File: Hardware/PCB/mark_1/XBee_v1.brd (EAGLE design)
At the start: 30.5 x 34.3 mm, 17 parts, among them IC1 4050, IC2 LM1117S

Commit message: 
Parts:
- renumbered U$1 to IC3
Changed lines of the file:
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@@
 <attribute name="VALUE" x="22.86" y="14.605" size="1.27" layer="28" rot="MR270"/>
 </element>
-<element name="U$1" library="mark_1" package="XBEE-1" value="XBEE-1B1" x="15.24" y="5.08" smashed="yes"/>
+<element name="IC3" library="mark_1" package="XBEE-1" value="XBEE-1B1" x="15.24" y="5.08" smashed="yes"/>
 <element name="JP1" library="mark_1" package="1X02" value="" x="7.62" y="11.43" smashed="yes" rot="R270">
 <attribute name="VALUE" x="4.445" y="13.97" size="1.27" layer="27" rot="R270"/>
@@
 <attribute name="VALUE" x="24.13" y="29.464" size="1.27" layer="28" ratio="10" rot="MR0"/>
 </element>
-<element name="JP2" library="mark_1" package="1X01" value="TXD" x="7.62" y="25.4" smashed="yes" rot="R270">
-<attribute name="VALUE" x="8.89" y="24.765" size="1.27" layer="27"/>
-</element>
-<element name="JP3" library="mark_1" package="1X01" value="RXD" x="7.62" y="22.86" smashed="yes" rot="R270">
-<attribute name="VALUE" x="8.89" y="22.225" size="1.27" layer="27"/>
-</element>
-<element name="JP4" library="mark_1" package="1X01" value="RST" x="7.62" y="20.32" smashed="yes" rot="R270">
-<attribute name="VALUE" x="8.89" y="19.685" size="1.27" layer="27"/>
-</element>
-<element name="JP5" library="mark_1" package="1X01" value="RSSI" x="7.62" y="15.24" smashed="yes">
-<attribute name="VALUE" x="8.89" y="14.605" size="1.27" layer="27"/>
-</element>
-<element name="JP6" library="mark_1" package="1X01" value="DTR" x="7.62" y="17.78" smashed="yes" rot="R270">
-<attribute name="VALUE" x="8.89" y="17.145" size="1.27" layer="27"/>
-</element>
-<element name="JP7" library="mark_1" package="1X01" value="CTS" x="7.62" y="5.08" smashed="yes" rot="R90">
-<attribute name="VALUE" x="8.89" y="4.445" size="1.27" layer="27"/>
-</element>
-<element name="JP8" library="mark_1" package="1X01" value="RTS" x="7.62" y="7.62" smashed="yes" rot="R270">
-<attribute name="VALUE" x="8.89" y="6.985" size="1.27" layer="27"/>
-</element>
+<element name="JP2" library="mark_1" package="1X01" value="TXD" x="7.62" y="25.4" smashed="yes" rot="R270"/>
+<element name="JP3" library="mark_1" package="1X01" value="RXD" x="7.62" y="22.86" smashed="yes" rot="R270"/>
+<element name="JP4" library="mark_1" package="1X01" value="RST" x="7.62" y="20.32" smashed="yes" rot="R270"/>
+<element name="JP5" library="mark_1" package="1X01" value="RSSI" x="7.62" y="15.24" smashed="yes"/>
+<element name="JP6" library="mark_1" package="1X01" value="DTR" x="7.62" y="17.78" smashed="yes" rot="R270"/>
+<element name="JP7" library="mark_1" package="1X01" value="CTS" x="7.62" y="5.08" smashed="yes" rot="R90"/>
+<element name="JP8" library="mark_1" package="1X01" value="RTS" x="7.62" y="7.62" smashed="yes" rot="R270"/>
 </elements>
 <signals>
@@
 <contactref element="JP1" pad="2"/>
 <contactref element="LED1" pad="K"/>
-<contactref element="U$1" pad="10"/>
+<contactref element="IC3" pad="10"/>
 <contactref element="LED2" pad="K"/>
 <contactref element="IC1" pad="8"/>
@@
 <contactref element="IC2" pad="2"/>
 <contactref element="IC2" pad="4"/>
-<contactref element="U$1" pad="1"/>
+<contactref element="IC3" pad="1"/>
 <contactref element="IC1" pad="1"/>
 <contactref element="C1" pad="2"/>
@@
 </signal>
 <signal name="N$3">
-<contactref element="U$1" pad="3"/>
+<contactref element="IC3" pad="3"/>
 <contactref element="IC1" pad="6"/>
 <wire x1="14.7066" y1="22.86" x2="10.795" y2="22.86" width="0.4064" layer="16"/>
@@
 </signal>
 <signal name="N$4">
-<contactref element="U$1" pad="5"/>
+<contactref element="IC3" pad="5"/>
 <contactref element="IC1" pad="4"/>
 <wire x1="4.24" y1="17.08" x2="4.38" y2="17.08" width="0.4064" layer="16"/>
@@
 </signal>
 <signal name="RSSI">
-<contactref element="U$1" pad="6"/>
+<contactref element="IC3" pad="6"/>
 <contactref element="R1" pad="2"/>
 <contactref element="JP5" pad="1"/>
@@
 </signal>
 <signal name="N$7">
-<contactref element="U$1" pad="9"/>
+<contactref element="IC3" pad="9"/>
 <contactref element="IC1" pad="2"/>
 <wire x1="12.7" y1="17.78" x2="14.7066" y2="17.78" width="0.4064" layer="16"/>
@@
 </signal>
 <signal name="N$8">
-<contactref element="U$1" pad="16"/>
+<contactref element="IC3" pad="16"/>
 <contactref element="IC1" pad="10"/>
 <wire x1="26.24" y1="17.08" x2="25.465" y2="17.08" width="0.4064" layer="16"/>
@@
 </signal>
 <signal name="N$10">
-<contactref element="U$1" pad="15"/>
+<contactref element="IC3" pad="15"/>
 <contactref element="R2" pad="2"/>
 <wire x1="26.24" y1="15.08" x2="27.145" y2="15.08" width="0.4064" layer="16"/>
@@
 </signal>
 <signal name="TXD">
-<contactref element="U$1" pad="2"/>
+<contactref element="IC3" pad="2"/>
 <contactref element="JP2" pad="1"/>
 <wire x1="4.24" y1="23.08" x2="5.3" y2="23.08" width="0.4064" layer="16"/>
@@
 </signal>
 <signal name="CTS">
-<contactref element="U$1" pad="12"/>
+<contactref element="IC3" pad="12"/>
 <contactref element="JP7" pad="1"/>
 <wire x1="7.62" y1="5.08" x2="7.62" y2="2.54" width="0.4064" layer="16"/>

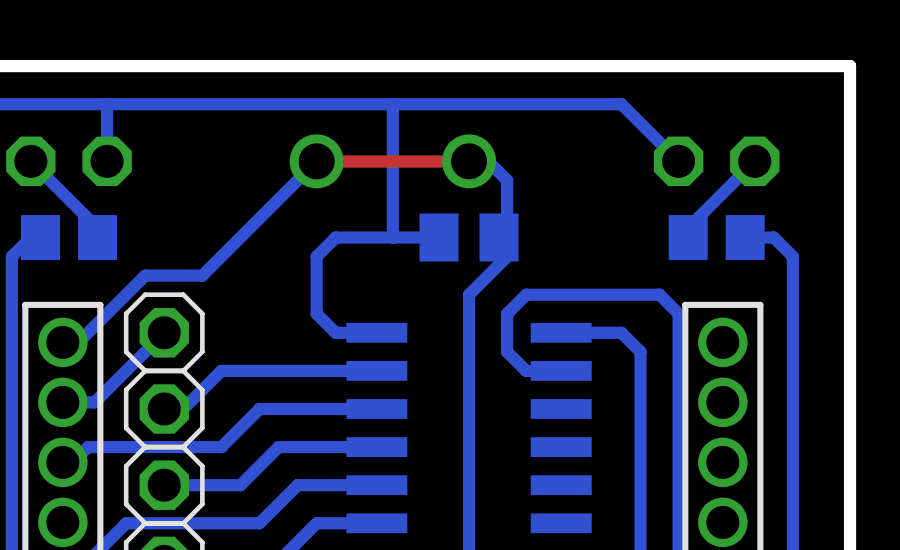
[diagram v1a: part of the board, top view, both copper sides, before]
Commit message: 
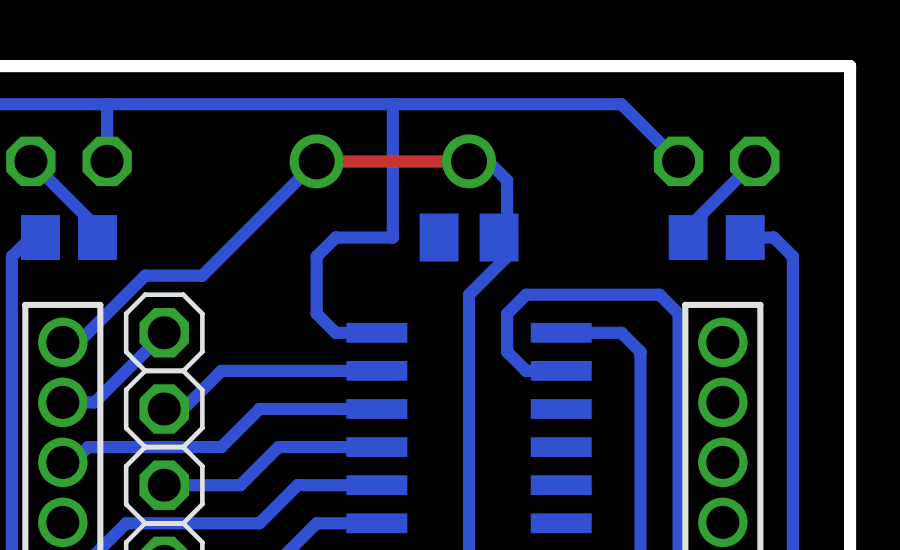
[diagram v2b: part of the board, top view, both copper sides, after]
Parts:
- IC2: value LM1117S -> LM1117-3.3
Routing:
- net +3V3: track 57.3 -> 55.2 mm
- net GND: track 84.2 -> 82.7 mm
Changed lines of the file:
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@@
 </autorouter>
 <elements>
-<element name="IC1" library="mark_1" package="SO16" value="4050" x="17.78" y="20.955" smashed="yes" rot="MR90">
-<attribute name="VALUE" x="17.145" y="21.336" size="1.27" layer="28" ratio="10" rot="MR90"/>
-<attribute name="NAME" x="17.145" y="17.018" size="1.27" layer="26" ratio="10" rot="MR90"/>
-</element>
+<element name="IC1" library="mark_1" package="SO16" value="4050" x="17.78" y="20.955" smashed="yes" rot="MR90"/>
 <element name="C1" library="mark_1" package="C0805K" value="100nF" x="17.78" y="28.575" rot="MR180"/>
-<element name="IC2" library="mark_1" package="SOT223" value="LM1117S" x="17.78" y="6.985" smashed="yes" rot="MR90">
+<element name="IC2" library="mark_1" package="SOT223" value="LM1117-3.3" x="17.78" y="6.985" smashed="yes" rot="MR90">
 <attribute name="NAME" x="17.8308" y="3.81" size="1.016" layer="26" rot="MR90"/>
 <attribute name="VALUE" x="16.4592" y="3.81" size="1.016" layer="28" rot="MR90"/>
@@
 <contactref element="LED2" pad="K"/>
 <contactref element="IC1" pad="8"/>
-<contactref element="C1" pad="1"/>
 <wire x1="15.24" y1="25.4" x2="14.7066" y2="25.4" width="0.254" layer="16"/>
 <wire x1="4.24" y1="7.08" x2="4.54" y2="7.08" width="0.4064" layer="16"/>
@@
 <wire x1="1.905" y1="6.985" x2="1.27" y2="7.62" width="0.4064" layer="16"/>
 <wire x1="1.27" y1="7.62" x2="1.27" y2="32.385" width="0.4064" layer="16"/>
-<wire x1="15.24" y1="28.575" x2="16.78" y2="28.575" width="0.4064" layer="16"/>
 <wire x1="15.24" y1="28.575" x2="15.24" y2="33.02" width="0.4064" layer="16"/>
 <wire x1="5.715" y1="33.02" x2="1.905" y2="33.02" width="0.4064" layer="16"/>
@@
 <wire x1="12.7" y1="27.94" x2="13.335" y2="28.575" width="0.4064" layer="16"/>
 <wire x1="13.335" y1="28.575" x2="15.24" y2="28.575" width="0.4064" layer="16"/>
+<contactref element="C1" pad="1"/>
+<wire x1="15.24" y1="28.575" x2="16.78" y2="28.575" width="0" layer="19" extent="16-16"/>
 </signal>
 <signal name="+3V3">
@@
 <contactref element="IC3" pad="1"/>
 <contactref element="IC1" pad="1"/>
-<contactref element="C1" pad="2"/>
-<wire x1="18.78" y1="28.575" x2="18.78" y2="28.94" width="0.4064" layer="16"/>
-<wire x1="19.05" y1="29.21" x2="18.78" y2="28.575" width="0.254" layer="16"/>
 <wire x1="21.59" y1="7.62" x2="20.955" y2="7.62" width="0.4064" layer="16"/>
 <wire x1="20.955" y1="7.62" x2="20.93" y2="6.985" width="0.4064" layer="16"/>
@@
 <wire x1="14.7066" y1="16.51" x2="17.78" y2="16.51" width="0.4064" layer="16"/>
 <wire x1="17.78" y1="16.51" x2="17.78" y2="26.67" width="0.4064" layer="16"/>
-<wire x1="18.78" y1="28.575" x2="18.78" y2="28.21" width="0.4064" layer="16"/>
 <wire x1="4.24" y1="25.08" x2="4.76" y2="25.08" width="0.4064" layer="16"/>
 <wire x1="4.76" y1="25.08" x2="6.985" y2="27.305" width="0.4064" layer="16"/>
@@
 <wire x1="18.415" y1="31.115" x2="19.05" y2="30.48" width="0.4064" layer="16"/>
 <wire x1="19.05" y1="30.48" x2="19.05" y2="28.575" width="0.4064" layer="16"/>
-<wire x1="18.78" y1="28.575" x2="19.05" y2="28.575" width="0.4064" layer="16"/>
 <wire x1="17.78" y1="26.67" x2="19.05" y2="27.94" width="0.4064" layer="16"/>
 <wire x1="19.05" y1="27.94" x2="19.05" y2="28.305" width="0.4064" layer="16"/>
-<wire x1="19.05" y1="28.305" x2="18.78" y2="28.575" width="0.4064" layer="16"/>
 <wire x1="8.89" y1="27.305" x2="6.985" y2="27.305" width="0.4064" layer="16"/>
+<contactref element="C1" pad="2"/>
+<wire x1="19.05" y1="28.575" x2="18.78" y2="28.575" width="0" layer="19" extent="16-16"/>
+<wire x1="19.05" y1="28.305" x2="19.05" y2="28.575" width="0" layer="19" extent="16-16"/>
 </signal>
 <signal name="+5V">
